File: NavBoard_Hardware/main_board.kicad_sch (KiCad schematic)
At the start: 9 parts, among them J1 24Pin to 16Pin, J2 Teensy Ethernet, J3 Ethernet Jack w/ Magnetics

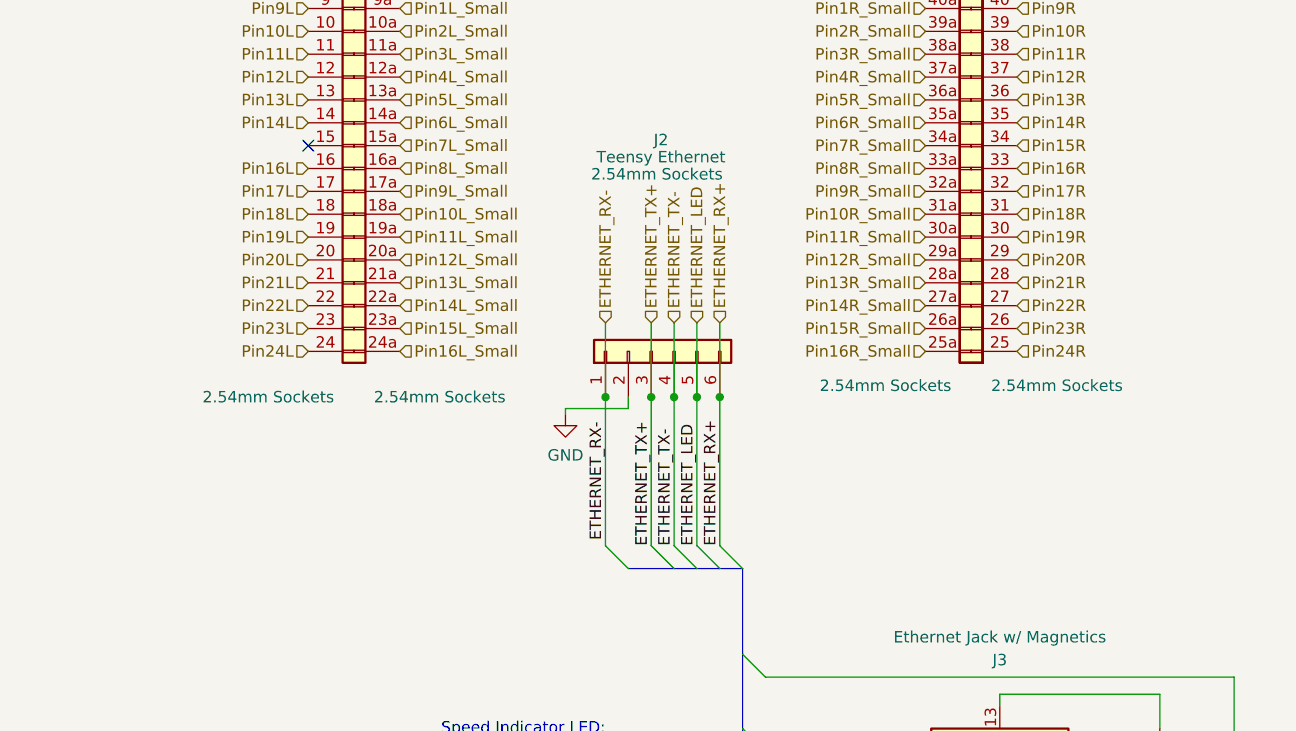
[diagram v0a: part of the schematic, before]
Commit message: Placed OKI SMD components, aligned ethernet pins
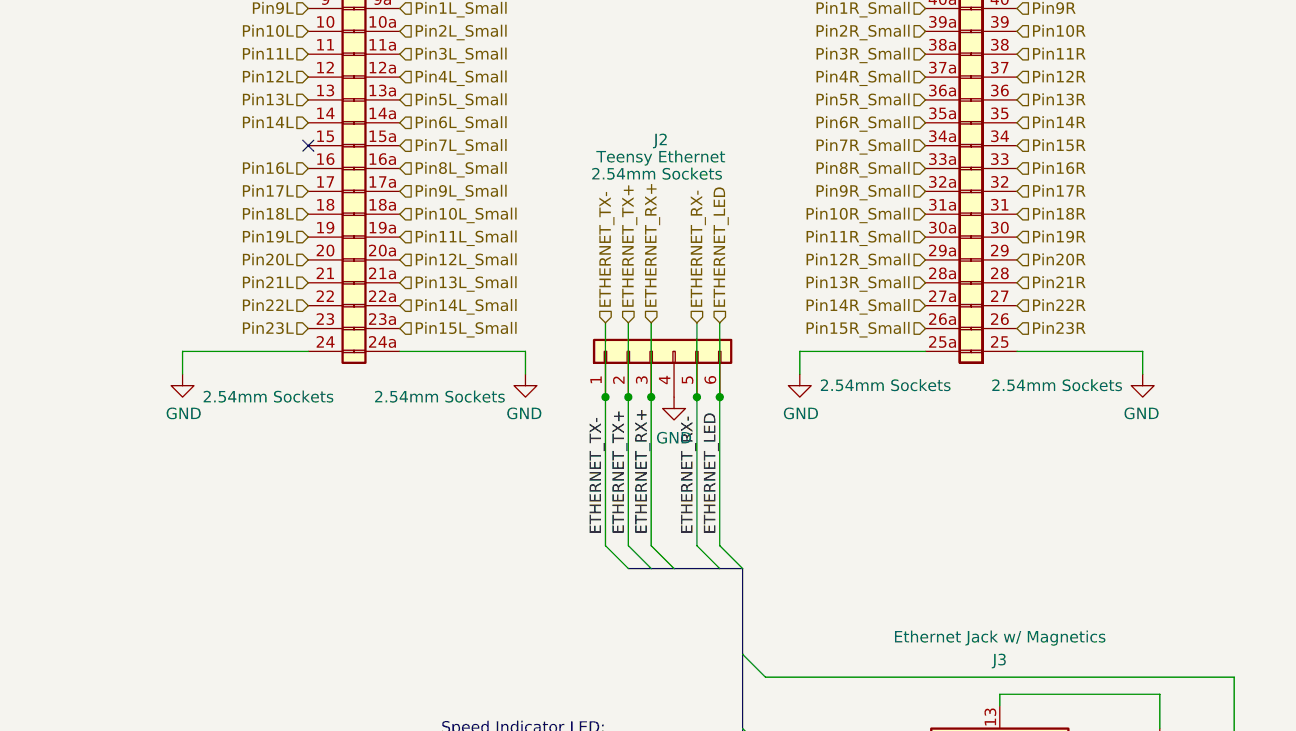
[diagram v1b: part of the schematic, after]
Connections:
- net Pin16L_Small is gone; now on net GND: J1.24a
- net Pin16R_Small is gone; now on net GND: J1.25a
- net Pin24L is gone; now on net GND: J1.24
- net Pin24R is gone; now on net GND: J1.25
- net ETHERNET_LED: now also J2.6 (Pin_6); no longer J2.5 (Pin_5)
- net ETHERNET_RX+: now also J2.3 (Pin_3); no longer J2.6 (Pin_6)
- net ETHERNET_RX-: now also J2.5 (Pin_5); no longer J2.1 (Pin_1)
- net ETHERNET_TX+: now also J2.2 (Pin_2); no longer J2.3 (Pin_3)
- net ETHERNET_TX-: now also J2.1 (Pin_1); no longer J2.4 (Pin_4)
- net GND: now also J2.4 (Pin_4); no longer J2.2 (Pin_2)

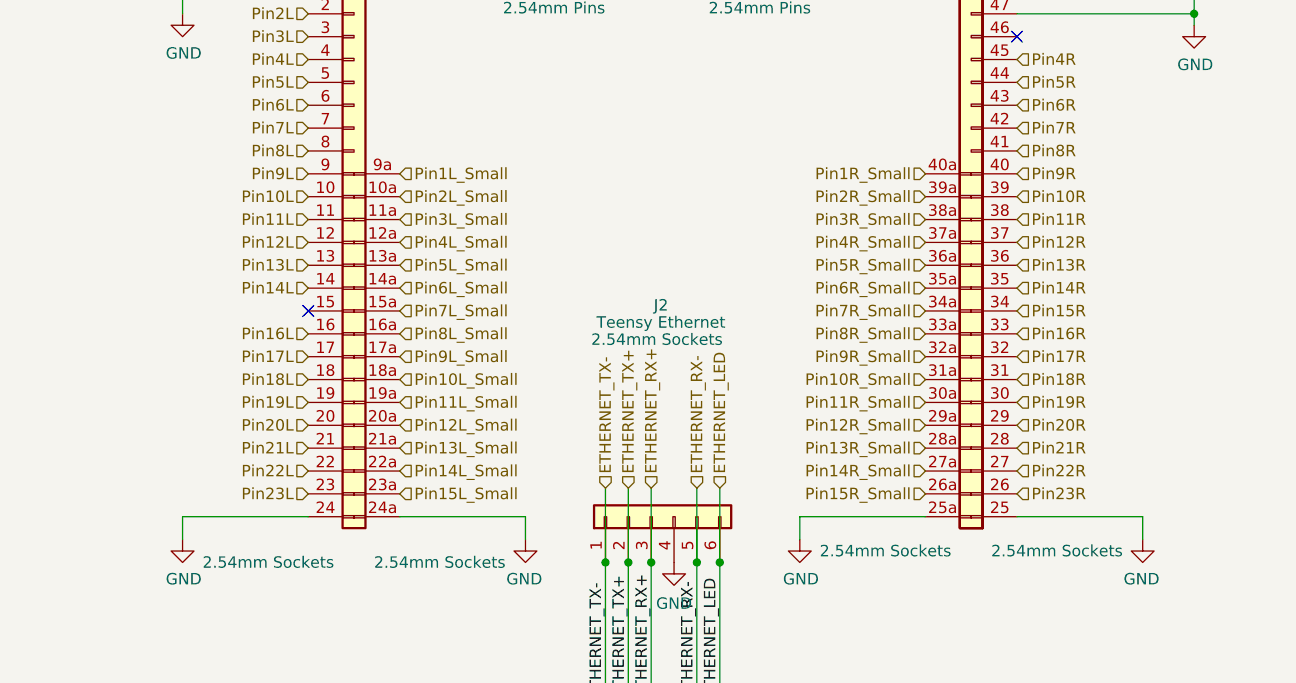
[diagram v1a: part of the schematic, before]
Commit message: Completed routing, added 3D models to IMUs
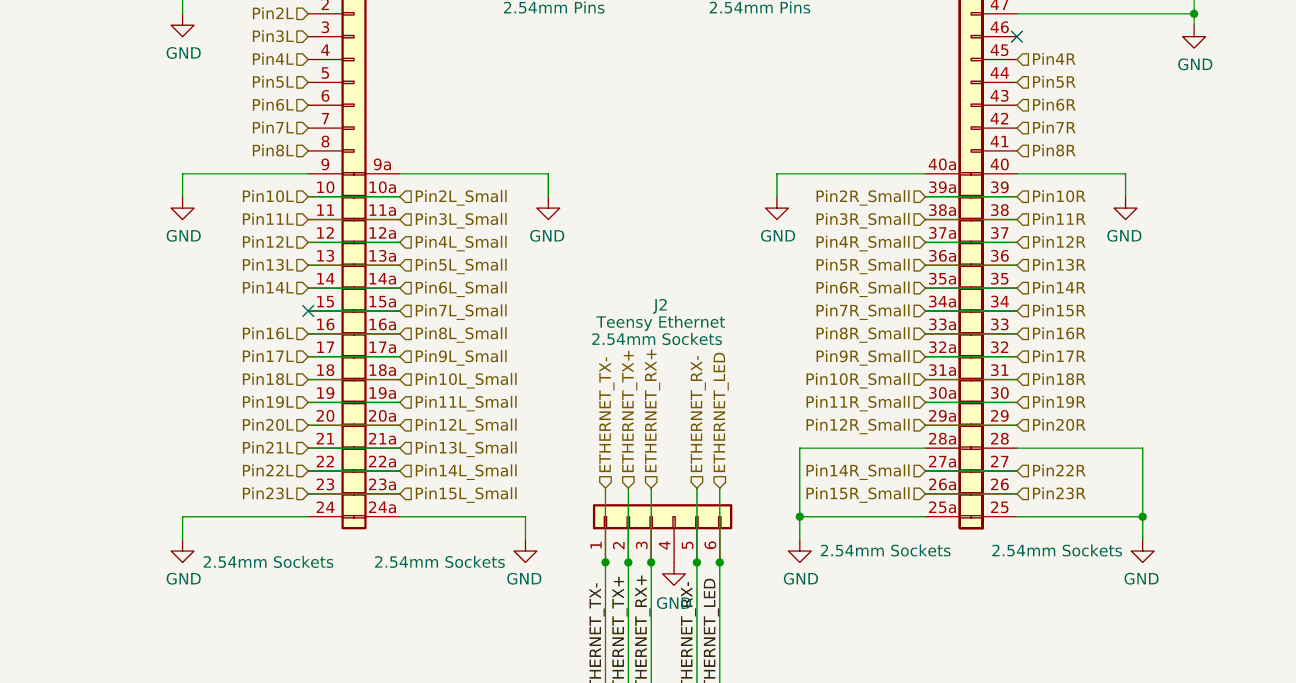
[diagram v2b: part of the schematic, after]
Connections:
- net Pin13R_Small is gone; now on net GND: J1.28a
- net Pin18L is gone; now on net Pin10L_Small: J1.18
- net Pin18R is gone; now on net Pin10R_Small: J1.31
- net Pin19L is gone; now on net Pin11L_Small: J1.19
- net Pin19R is gone; now on net Pin11R_Small: J1.30
- net Pin1L_Small is gone; now on net GND: J1.9a
- net Pin1R_Small is gone; now on net GND: J1.40a
- net Pin20L is gone; now on net Pin12L_Small: J1.20
- net Pin20R is gone; now on net Pin12R_Small: J1.29
- net Pin21L is gone; now on net Pin13L_Small: J1.21
- net Pin21R is gone; now on net GND: J1.28
- net Pin22L is gone; now on net Pin14L_Small: J1.22
- net Pin22R is gone; now on net Pin14R_Small: J1.27
- net Pin23L is gone; now on net Pin15L_Small: J1.23
- net Pin23R is gone; now on net Pin15R_Small: J1.26
- net Pin2L_Small is gone; now on net Pin10L: J1.10a
- net Pin2R_Small is gone; now on net Pin10R: J1.39a
- net Pin3L_Small is gone; now on net Pin11L: J1.11a
- net Pin3R_Small is gone; now on net Pin11R: J1.38a
- net Pin4L_Small is gone; now on net Pin12L: J1.12a
- net Pin4R_Small is gone; now on net Pin12R: J1.37a
- net Pin5L_Small is gone; now on net Pin13L: J1.13a
- net Pin5R_Small is gone; now on net Pin13R: J1.36a
- net Pin6L_Small is gone; now on net Pin14L: J1.14a
- net Pin6R_Small is gone; now on net Pin14R: J1.35a
- net Pin7R_Small is gone; now on net Pin15R: J1.34a
- net Pin8L_Small is gone; now on net Pin16L: J1.16a
- net Pin8R_Small is gone; now on net Pin16R: J1.33a
- net Pin9L is gone; now on net GND: J1.9
- net Pin9L_Small is gone; now on net Pin17L: J1.17a
- net Pin9R is gone; now on net GND: J1.40
- net Pin9R_Small is gone; now on net Pin17R: J1.32a
- net Pin7L_Small: now also J1.15

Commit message: Annotated schematic pages
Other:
- company: (none) -> Thomas Francois, Missouri S&T Mars Rover Design Team
- title: (none) -> MRDT NavBoard - Main Board
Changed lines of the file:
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@@
 (kicad_sch (version 20211123) (generator eeschema)
   (paper "A4")
+  (title_block
+    (title "MRDT NavBoard - Main Board")
+    (rev "1, 2023")
+    (company "Thomas Francois, Missouri S&T Mars Rover Design Team")
+    (comment 1 "Teensy daughter board")
+    (comment 2 "Contains an RJ45 connector and power supplies")
+  )
   (junction (at 86.995 127) (diameter 0) (color 0 0 0 0)
   )

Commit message: Initial changes and prototyping the new layout
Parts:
- added U5: Teensy4.1, teensy:Teensy41, symbol teensy:Teensy4.1
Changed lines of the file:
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@@
     (pin "48")
+  )
+  (symbol (lib_id "teensy:Teensy4.1") (at 234.95 104.775 0) (unit 1)
+    (in_bom yes) (on_board yes)
+    (property "Reference" "U5" (id 0) (at 234.95 39.9755 0))
+    (property "Value" "Teensy4.1" (id 1) (at 234.95 42.7506 0))
+    (property "Footprint" "teensy:Teensy41" (id 2) (at 224.79 94.615 0)
+      (effects (font (size 1.27 1.27)) hide)
+    )
+    (property "Datasheet" "https://www.pjrc.com/store/teensy41.html" (id 3) (at 224.79 94.615 0)
+      (effects (font (size 1.27 1.27)) hide)
+    )
+    (property "Left Headers" "2.54mm Pins" (id 4) (at 212.09 41.275 0))
+    (property "Right Headers" "2.54mm Pins" (id 5) (at 257.81 41.275 0))
+    (pin "10")
+    (pin "11")
+    (pin "12")
+    (pin "13")
+    (pin "14")
+    (pin "15")
+    (pin "16")
+    (pin "17")
+    (pin "18")
+    (pin "19")
+    (pin "20")
+    (pin "21")
+    (pin "22")
+    (pin "23")
+    (pin "24")
+    (pin "25")
+    (pin "26")
+    (pin "27")
+    (pin "28")
+    (pin "29")
+    (pin "30")
+    (pin "31")
+    (pin "32")
+    (pin "33")
+    (pin "35")
+    (pin "36")
+    (pin "37")
+    (pin "38")
+    (pin "39")
+    (pin "40")
+    (pin "41")
+    (pin "42")
+    (pin "43")
+    (pin "44")
+    (pin "45")
+    (pin "46")
+    (pin "47")
+    (pin "48")
+    (pin "49")
+    (pin "5")
+    (pin "50")
+    (pin "51")
+    (pin "52")
+    (pin "53")
+    (pin "54")
+    (pin "55")
+    (pin "56")
+    (pin "57")
+    (pin "58")
+    (pin "59")
+    (pin "6")
+    (pin "60")
+    (pin "61")
+    (pin "62")
+    (pin "63")
+    (pin "64")
+    (pin "65")
+    (pin "66")
+    (pin "67")
+    (pin "7")
+    (pin "8")
+    (pin "9")
+    (pin "1")
+    (pin "2")
+    (pin "3")
+    (pin "34")
+    (pin "4")
   )
   (symbol (lib_id "power:GND") (at 142.24 185.42 0) (unit 1)

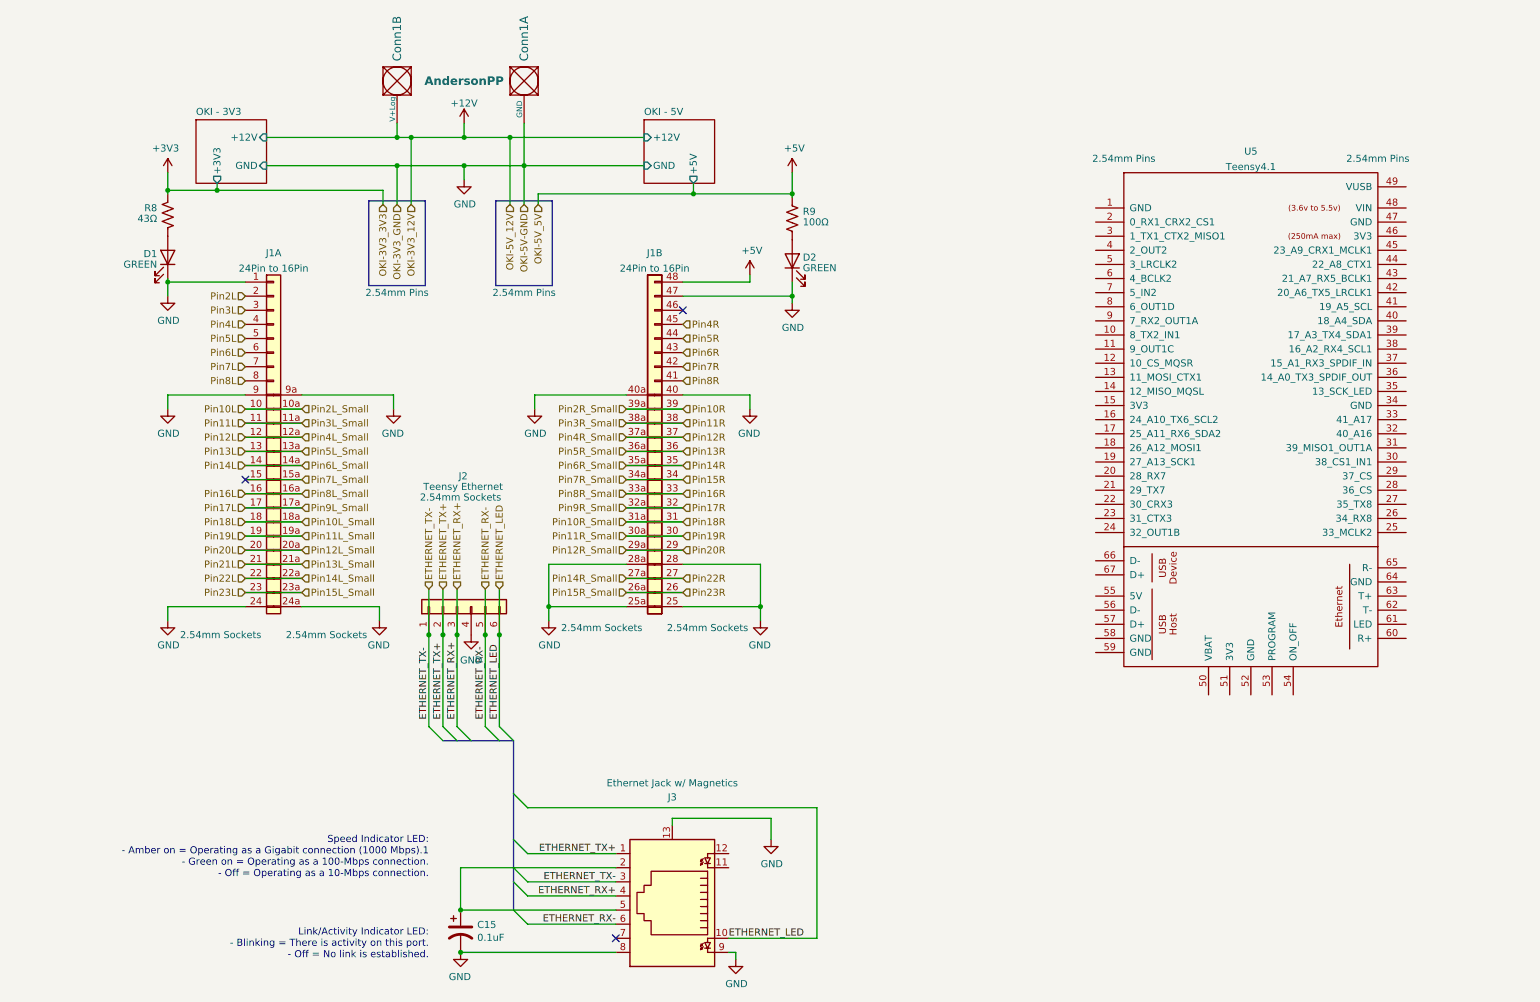
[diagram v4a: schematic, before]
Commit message: Rearranged schematic
I realize now that this is a dumb idea...
Going to redesign the board so the teensy just sits on top
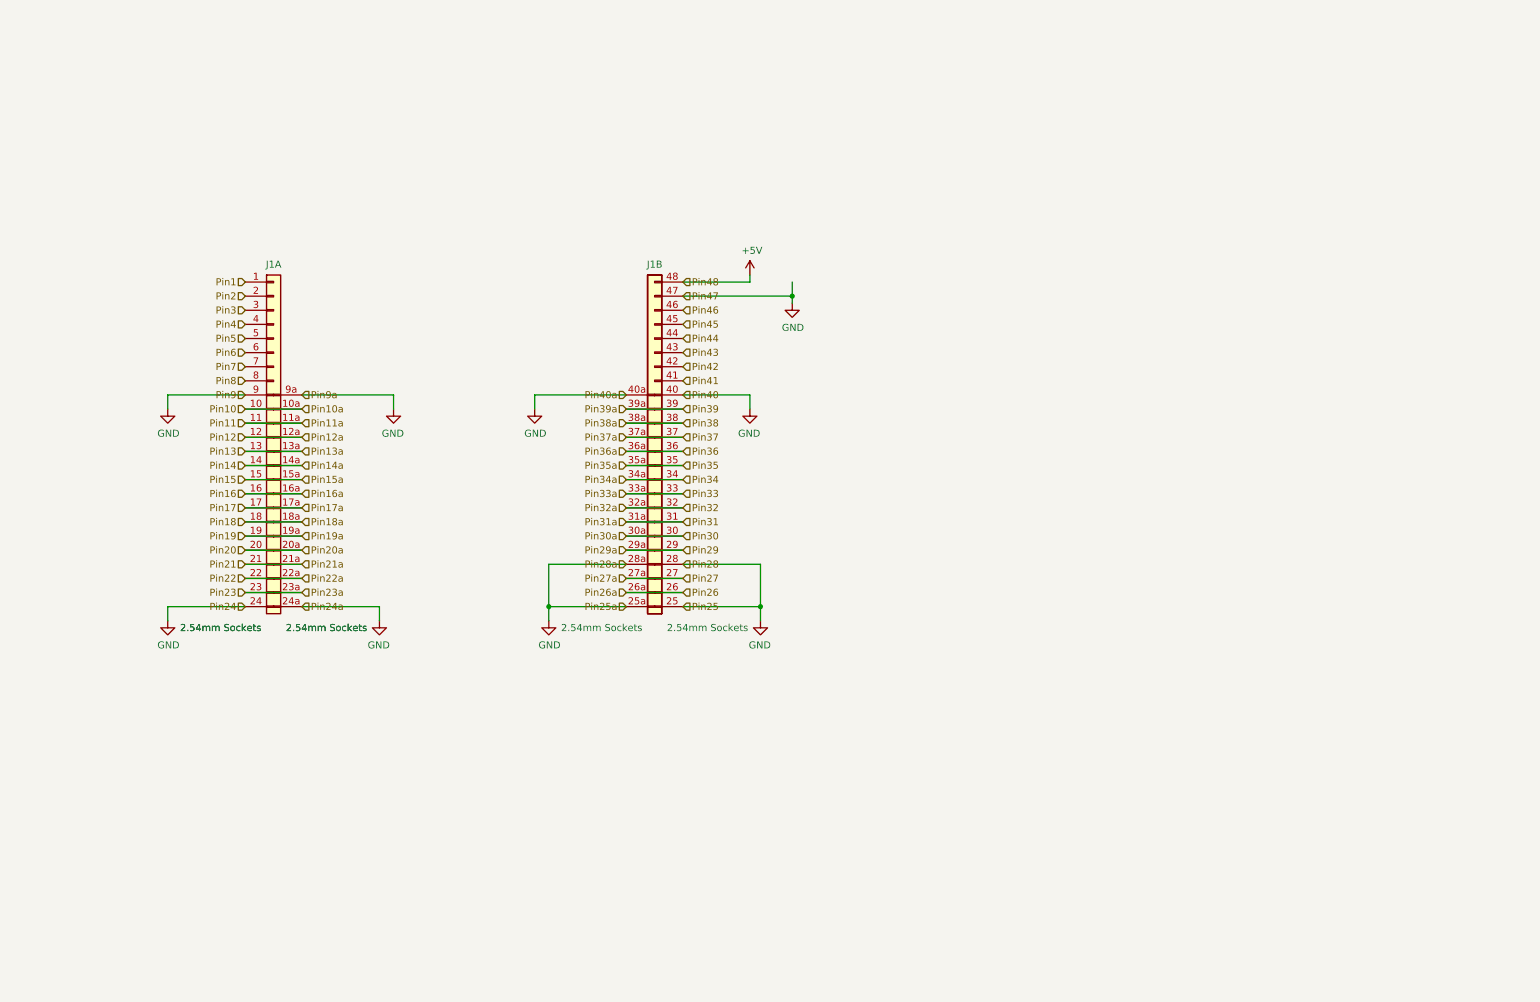
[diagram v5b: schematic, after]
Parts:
- removed C15: 0.1uF, Capacitor_SMD:C_0603_1608Metric_Pad1.08x0.95mm_HandSolder, symbol Device:C_Polarized_US
- removed Conn1: AndersonPP, MRDT_Connectors:Anderson_2_Horizontal_Side_by_Side, symbol MRDT_Connectors:AndersonPP
- removed D1, D2: GREEN, LED_SMD:LED_0603_1608Metric_Pad1.05x0.95mm_HandSolder, symbol Device:LED
- removed J2: Teensy Ethernet, Connector_PinSocket_2.54mm:PinSocket_2x03_P2.54mm_Vertical, symbol Connector_Generic:Conn_01x06
- removed J3: Ethernet Jack w/ Magnetics, Connector_RJ:RJ45_Cetus_J1B1211CCD_Horizontal, symbol Connector:8P8C_LED_Shielded
- removed R8: 43Ω, Resistor_SMD:R_0603_1608Metric_Pad0.98x0.95mm_HandSolder, symbol Device:R_US
- removed R9: 100Ω, Resistor_SMD:R_0603_1608Metric_Pad0.98x0.95mm_HandSolder, symbol Device:R_US
- removed U5: Teensy4.1, teensy:Teensy41, symbol teensy:Teensy4.1
- J1: value 24Pin to 16Pin -> 24Pin_To_16Pin_2.54mm_Separate_Pins_Alt_2; symbol Nav_Board:24Pin_To_16Pin_2.54mm_Separate_Pins_Alt -> Nav_Board:24Pin_To_16Pin_2.54mm_Separate_Pins_Alt_2
- J1: value 24Pin to 16Pin -> 24Pin_To_16Pin_2.54mm_Separate_Pins_Alt_2; symbol Nav_Board:24Pin_To_16Pin_2.54mm_Separate_Pins_Alt -> Nav_Board:24Pin_To_16Pin_2.54mm_Separate_Pins_Alt_2; Inner Header Types (none) -> 2.54mm Sockets; Outer Header Types (none) -> 2.54mm Sockets
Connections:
- net GND: no longer J1.1
- net Pin46: now reaches J1.46
- net Pin10L renamed Pin10
- net Pin10L_Small renamed Pin18
- net Pin10R renamed Pin39
- net Pin10R_Small renamed Pin31
- net Pin11L renamed Pin11
- net Pin11L_Small renamed Pin19
- net Pin11R renamed Pin38
- net Pin11R_Small renamed Pin30
- net Pin12L renamed Pin12
- net Pin12L_Small renamed Pin20
- net Pin12R renamed Pin37
- net Pin12R_Small renamed Pin29
- net Pin13L renamed Pin13
- net Pin13L_Small renamed Pin21
- net Pin13R renamed Pin36
- net Pin14L renamed Pin14
- net Pin14L_Small renamed Pin22
- net Pin14R renamed Pin35
- net Pin14R_Small renamed Pin27
- net Pin15L_Small renamed Pin23
- net Pin15R renamed Pin34
- net Pin15R_Small renamed Pin26
- net Pin16L renamed Pin16
- net Pin16R renamed Pin33
- net Pin17L renamed Pin17
- net Pin17R renamed Pin32
- net Pin2L renamed Pin2
- net Pin3L renamed Pin3
- net Pin4L renamed Pin4
- net Pin4R renamed Pin45
- net Pin5L renamed Pin5
- net Pin5R renamed Pin44
- net Pin6L renamed Pin6
- net Pin6R renamed Pin43
- net Pin7L renamed Pin7
- net Pin7L_Small renamed Pin15
- net Pin7R renamed Pin42
- net Pin8L renamed Pin8
- net Pin8R renamed Pin41
- new net Pin1: J1.1
- no-connect marks 3 -> 0
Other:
- removed sheet OKI - 3V3
- removed sheet OKI - 5V
- note removed: "Link/Activity Indicator LED: - Blinking = There is activity on this port. - Off = No link is established."
- note removed: "Speed Indicator LED: - Amber on = Operating as a Gigabit connection (1000 Mbps).1 - Green on = Operating as a 100-Mbps connection. - Off = Operating as a 10-Mbps connection."
